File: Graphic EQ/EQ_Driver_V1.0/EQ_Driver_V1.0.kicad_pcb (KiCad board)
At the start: 2 copper layers, 127 x 57.2 mm, 35 parts, among them Q1 MPSA63, Q2 MPSA70, Q3 MPSA70, Q4 MPSA20

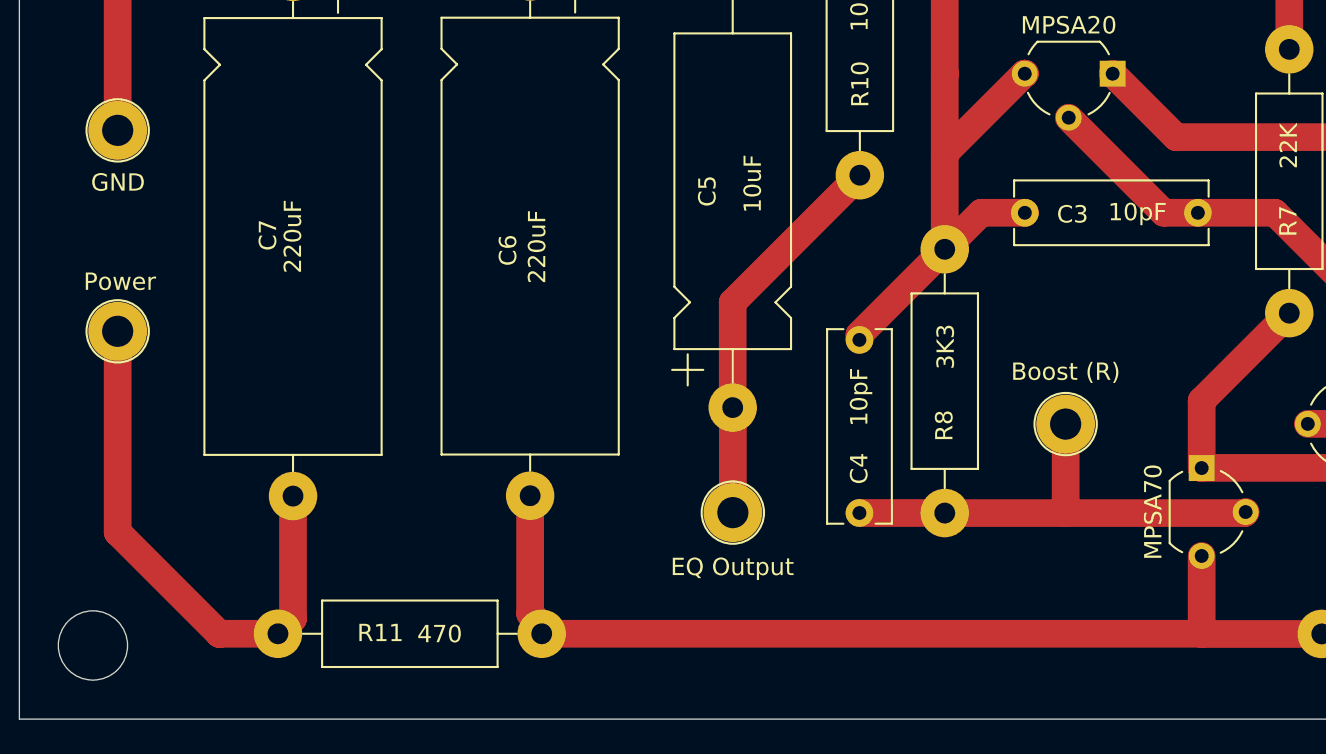
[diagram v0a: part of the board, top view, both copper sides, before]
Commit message: Started Power Supply Board, Made EQ Driver Changes
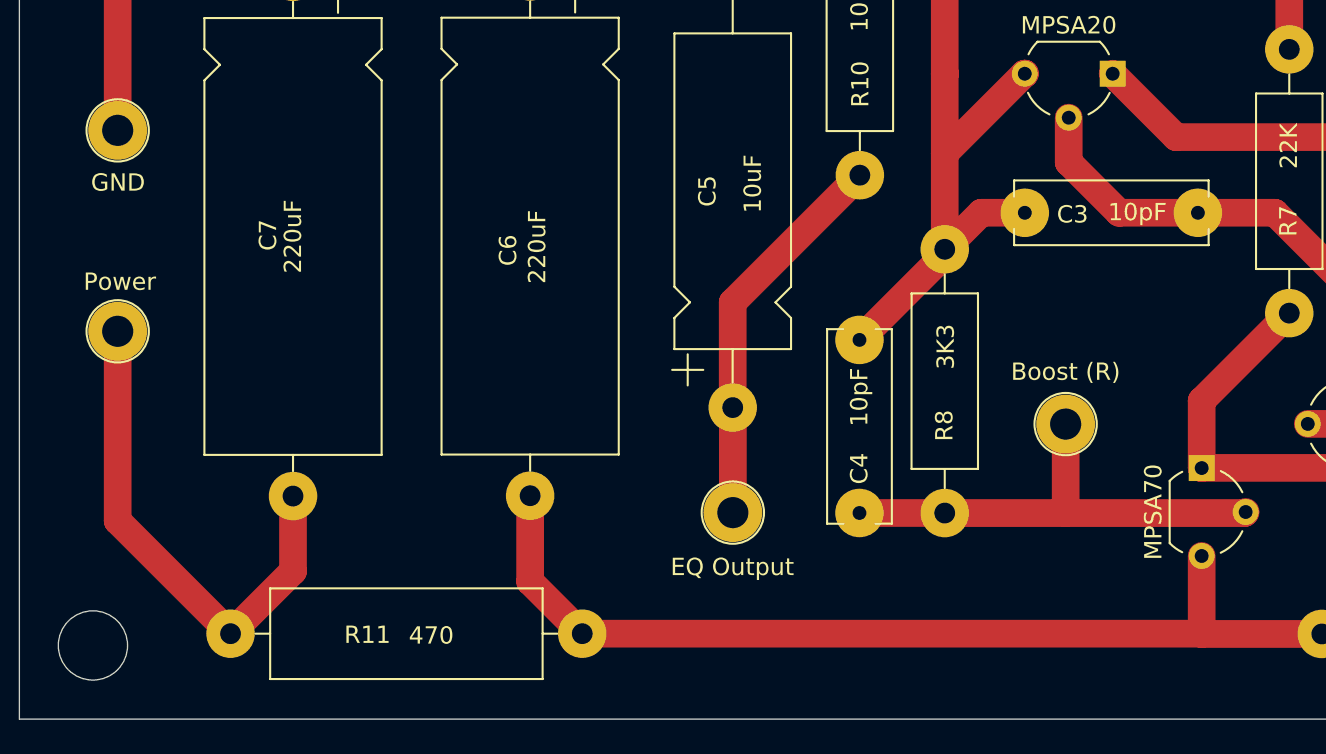
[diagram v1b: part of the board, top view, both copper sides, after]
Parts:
- R11: footprint Resistor_THT:R_Axial_DIN0411_L9.9mm_D3.6mm_P15.24mm_Horizontal -> Resistor_THT:R_Axial_DIN0516_L15.5mm_D5.0mm_P20.32mm_Horizontal
- moved R11 2.34 mm to (110.3, 117.6)
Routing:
- net Net-(C7-Pad2): track 31.6 -> 29.6 mm
- net Net-(Q2-C): track 25.7 -> 27.2 mm
- net Net-(Q1-C): track 123.0 -> 121.7 mm

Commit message: small updates
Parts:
- moved TP5 2.12 mm to (83.4, 98.0)
- moved TP6 1.49 mm to (83.4, 90.0)
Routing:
- net Net-(C7-Pad2): track 29.6 -> 31.7 mm
- net GND: track 198.5 -> 200.0 mm
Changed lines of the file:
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@@
 			(psa4output no)
 			(plot_black_and_white yes)
-			(plotinvisibletext no)
 			(sketchpadsonfab no)
 			(plotpadnumbers no)
@@
 	(footprint "HiroFootprints:Out_Hole_3.4_1.8"
 		(layer "F.Cu")
-		(at 83.43 100.12)
+		(at 83.43 98)
 		(property "Reference" "TP5"
 			(at 0 -0.5 0)
@@
 	(footprint "HiroFootprints:Out_Hole_3.4_1.8"
 		(layer "F.Cu")
-		(at 83.43 88.51)
+		(at 83.43 90)
 		(property "Reference" "TP6"
 			(at 0 -0.5 0)
@@
 	)
 	(segment
-		(start 83.43 88.51)
-		(end 83.43 76.94)
-		(width 1.6)
-		(layer "F.Cu")
-		(net 2)
-	)
-	(segment
 		(start 185.2 74.23)
 		(end 185.2 82.29)
@@
 	)
 	(segment
+		(start 83.43 76.94)
+		(end 83.43 90)
+		(width 1.6)
+		(layer "F.Cu")
+		(net 2)
+	)
+	(segment
 		(start 151.09 76.36)
 		(end 151.09 70.39)
@@
 	(segment
 		(start 83.43 111.07)
-		(end 89.95 117.59)
+		(end 83.43 98)
 		(width 1.6)
 		(layer "F.Cu")
@@
 	)
 	(segment
-		(start 83.43 100.12)
-		(end 83.43 111.07)
+		(start 83.43 111.07)
+		(end 89.95 117.59)
 		(width 1.6)
 		(layer "F.Cu")

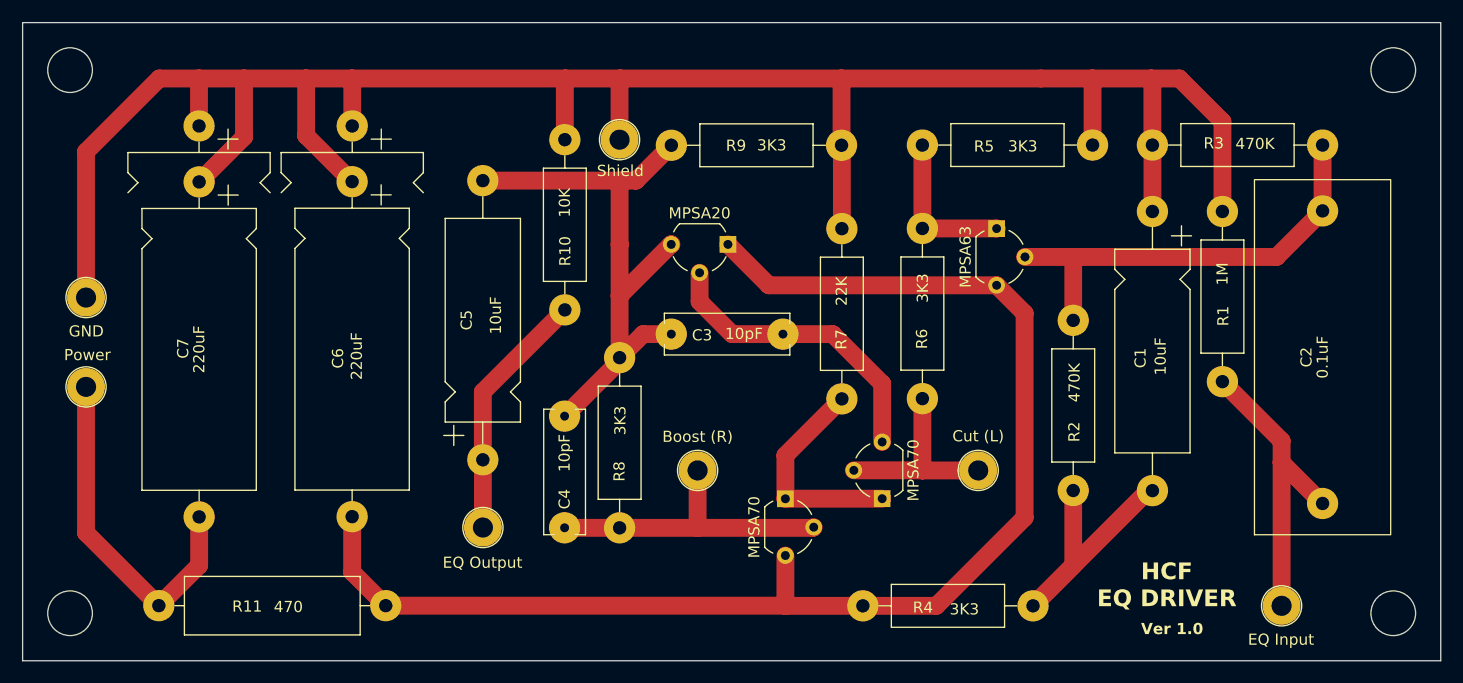
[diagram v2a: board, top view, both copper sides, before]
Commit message: Changed Driver Layout
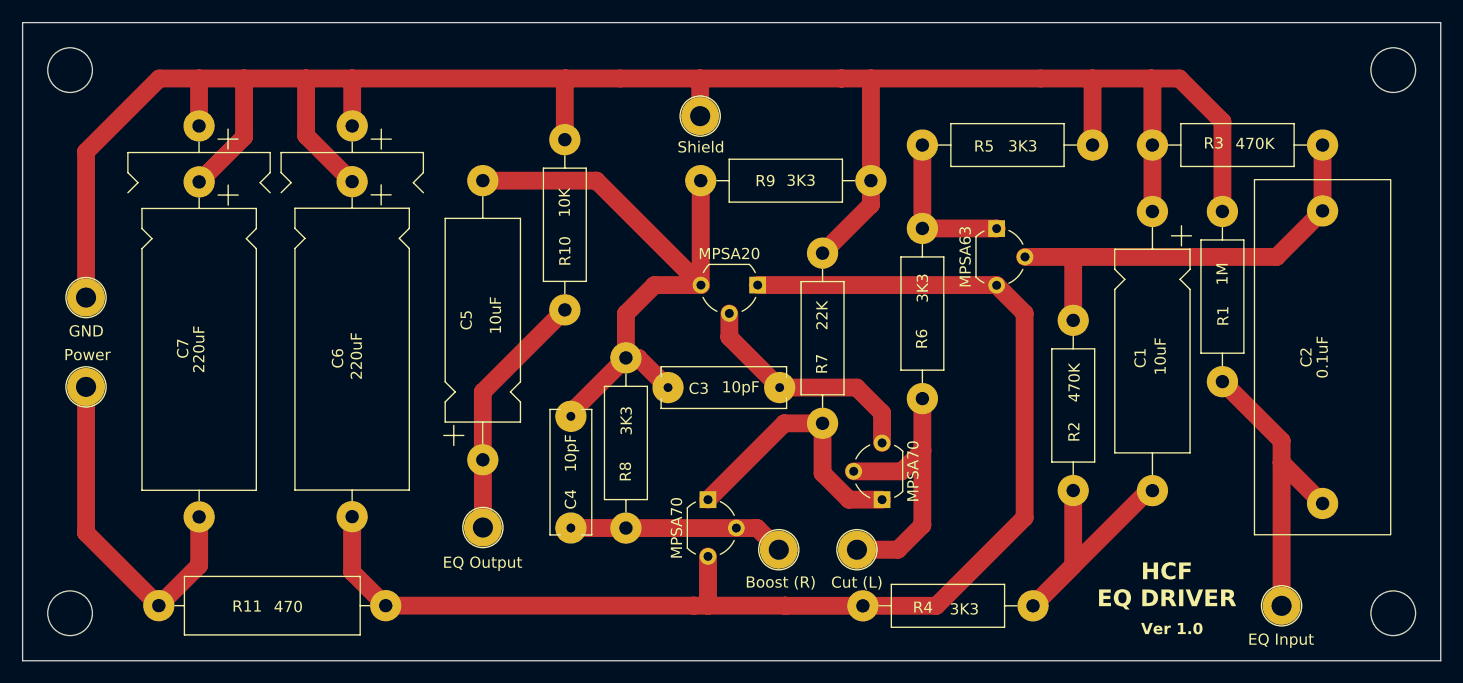
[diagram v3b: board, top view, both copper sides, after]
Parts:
- moved TP2 13.0 mm to (152.5, 112.6)
- moved TP3 10.2 mm to (145.5, 112.6)
- moved TP7 7.52 mm to (138.4, 73.8)
- moved Q3 6.93 mm to (139.1, 108.1)
- moved C3 4.80 mm to (145.6, 98.1)
- moved Q4 4.51 mm to (143.6, 88.9)
- moved R9 4.12 mm to (138.5, 79.5)
- moved R7 2.79 mm to (149.4, 101.3)
- moved C4 0.57 mm to (126.9, 110.6)
- moved R8 0.57 mm to (131.8, 110.6)
- moved Q2 0.09 mm to (154.7, 108.1)
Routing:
- net Net-(Q3-B): track 27.5 -> 19.4 mm
- net Net-(Q2-B): track 17.6 -> 25.0 mm
- net Net-(Q2-C): track 27.2 -> 21.3 mm
- net Net-(Q1-C): track 121.7 -> 117.4 mm
- net Net-(Q2-E): track 19.7 -> 23.9 mm
- net Net-(Q4-C): track 53.4 -> 56.7 mm
- net GND: track 200.0 -> 201.8 mm

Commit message: Added Solder Pads, Updated Power Supply Board
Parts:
- TP1, TP2, TP3, TP4, TP5, TP6, TP7: footprint HiroFootprints:Out_Hole_3.4_1.8 -> HiroFootprints:WirePad
- moved TP1 12.0 mm to (178.5, 116.6)
- moved TP2 11.0 mm to (161.1, 105.8)
- moved TP7 5.08 mm to (133.6, 75.4)
- moved TP3 1.74 mm to (145.8, 110.9)
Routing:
- net Net-(Q2-B): track 25.0 -> 15.4 mm
- net Net-(C2-Pad1): track 27.5 -> 31.0 mm
- net GND: track 201.8 -> 203.3 mm

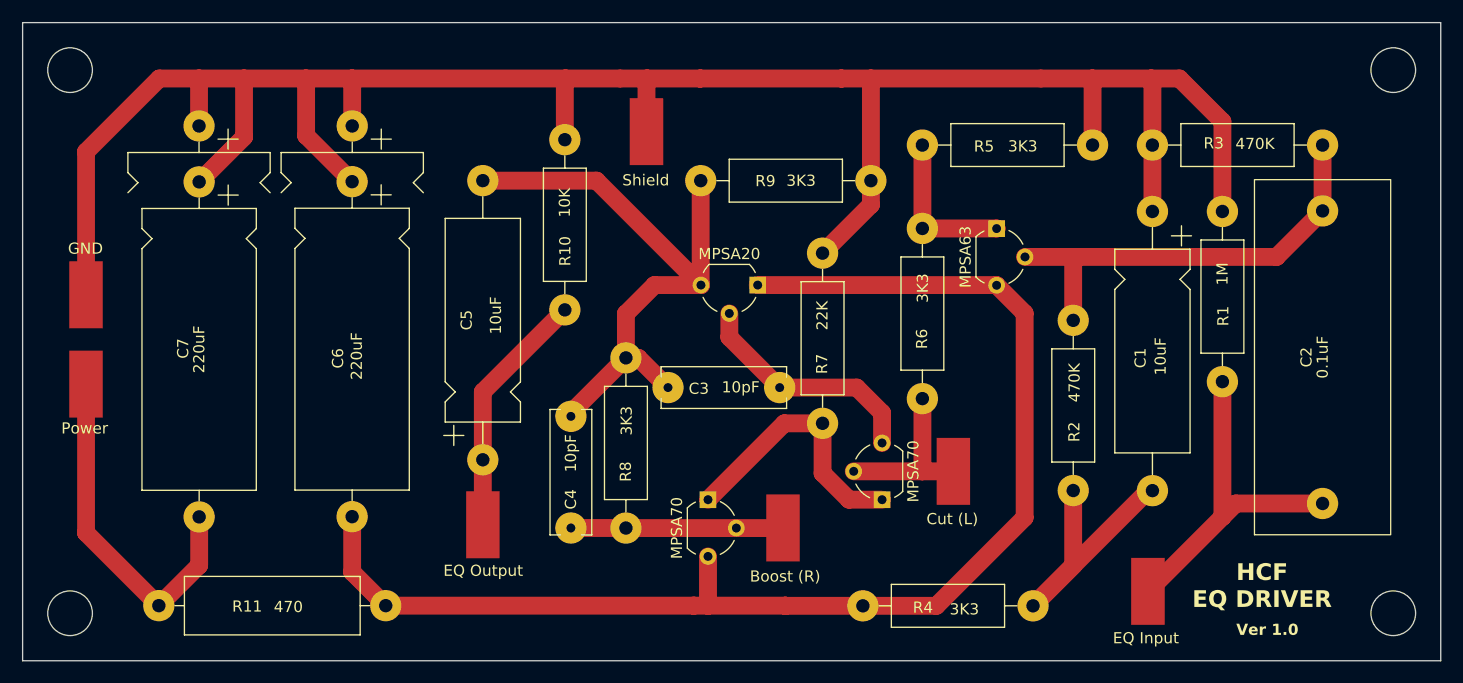
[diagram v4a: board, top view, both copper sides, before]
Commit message: increased trace width
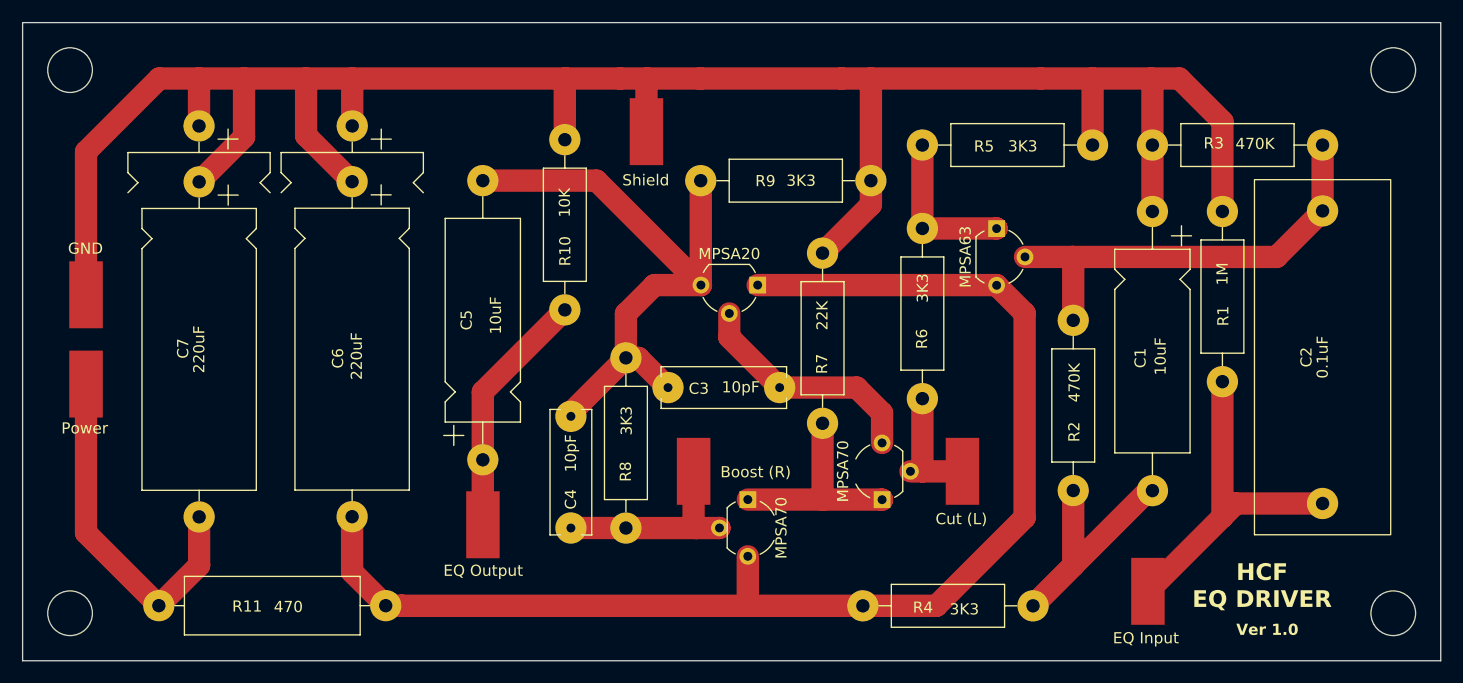
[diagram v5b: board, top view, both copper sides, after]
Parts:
- moved TP3 9.48 mm to (137.8, 105.8)
- moved Q3 3.57 mm to (142.7, 108.1)
- moved TP2 0.81 mm to (161.9, 105.8)
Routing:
- net Net-(Q2-E): track 23.9 -> 18.9 mm
- net Net-(Q2-B): track 15.4 -> 11.2 mm
- net Net-(Q3-B): track 19.0 -> 18.5 mm

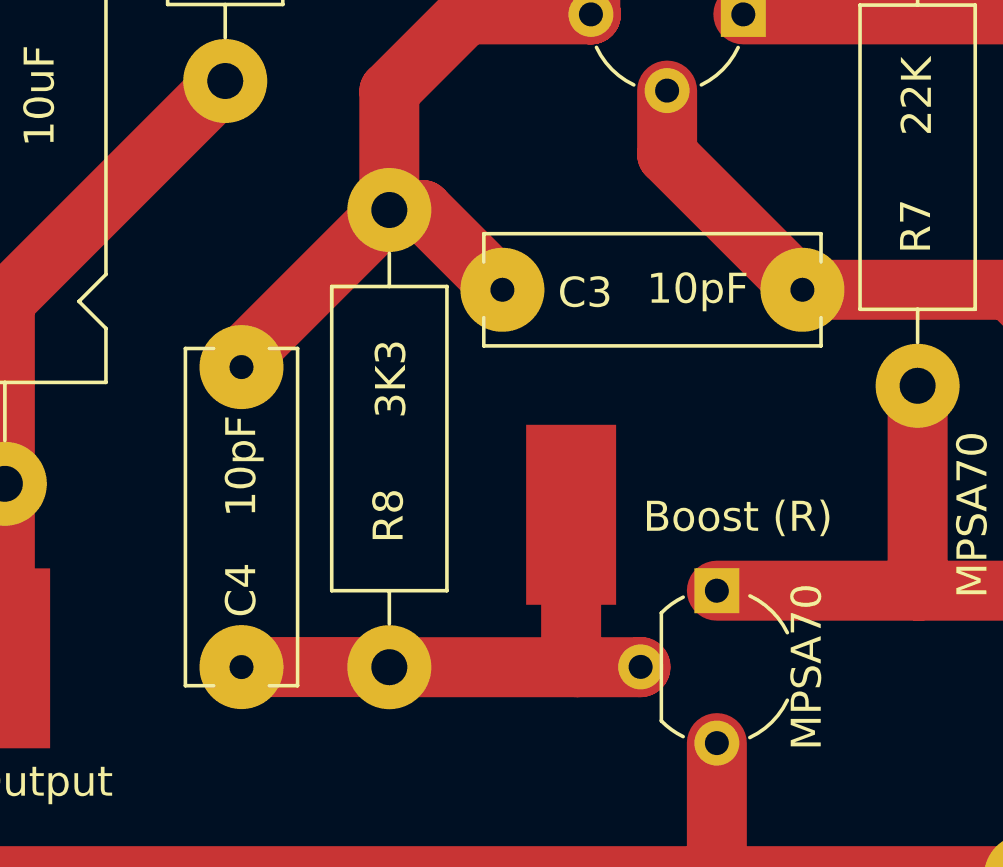
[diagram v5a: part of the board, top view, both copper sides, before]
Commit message: Updated Ceramic Capacitor Footprints
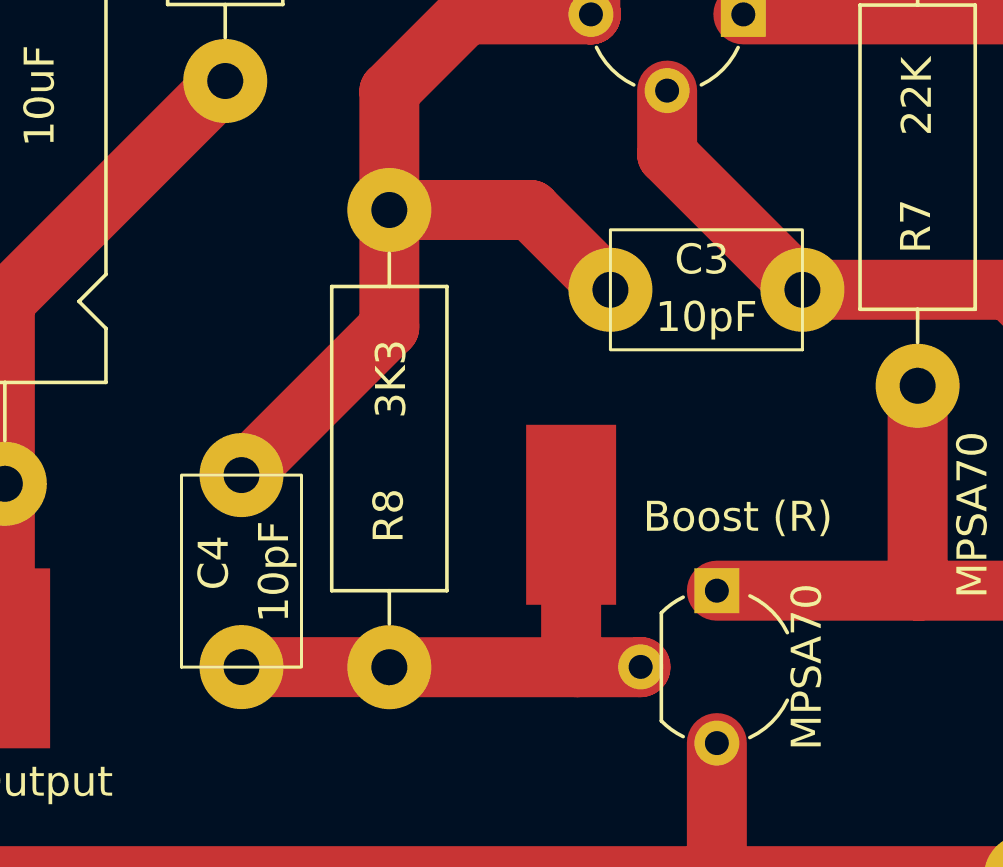
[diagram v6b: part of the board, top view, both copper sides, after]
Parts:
- C3, C4: footprint Capacitor_THT:C_Rect_L11.0mm_W3.5mm_P10.00mm_MKT -> HiroFootprints:10_47_120_180_250_500pF_1KV_Cer_6.4_4.0_6.4
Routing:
- net Net-(Q4-C): track 56.7 -> 63.9 mm
